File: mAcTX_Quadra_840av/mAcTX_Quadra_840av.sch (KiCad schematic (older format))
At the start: 24 parts, among them J1 ATX-24, J2 39-28-1223, Q1 Q_NPN_BCE

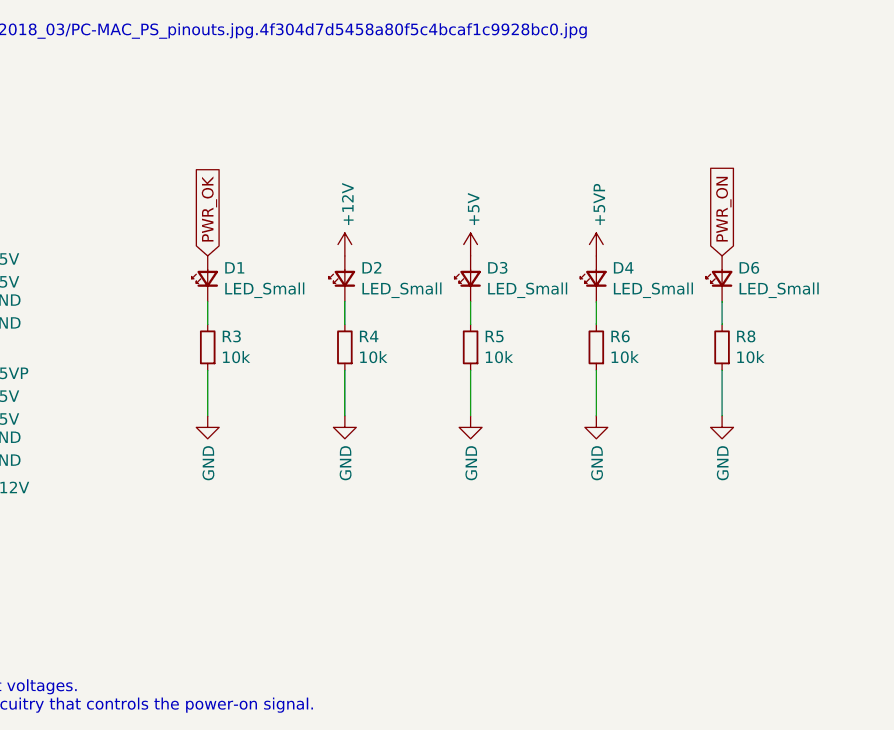
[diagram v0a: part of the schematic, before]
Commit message: Updated schematic to show which parts should not be populated
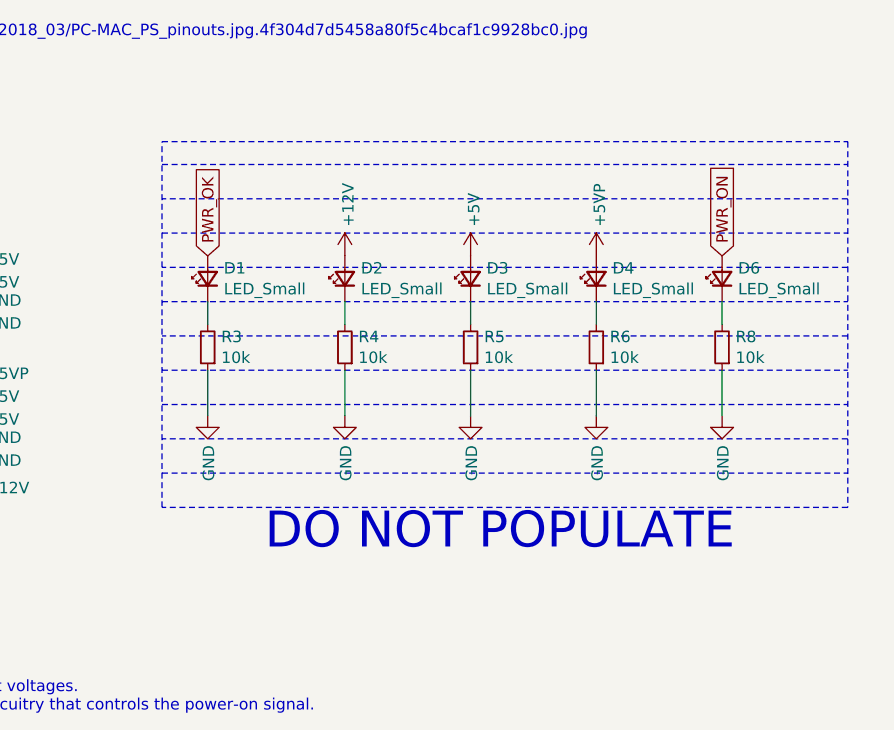
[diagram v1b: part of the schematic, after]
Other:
- note added: "DO NOT POPULATE"
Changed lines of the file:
@@
 	0    1    1    0
 $EndComp
+Wire Notes Line
+	7500 1100 10500 1100
+Wire Notes Line
+	10500 2700 7500 2700
+Wire Notes Line
+	7500 2700 7500 1100
+Wire Notes Line
+	7500 1200 10500 1200
+Wire Notes Line
+	10500 1350 7500 1350
+Wire Notes Line
+	7500 1500 10500 1500
+Wire Notes Line
+	10500 1650 7500 1650
+Wire Notes Line
+	7500 1800 10500 1800
+Wire Notes Line
+	10500 1950 7500 1950
+Wire Notes Line
+	7500 2100 10500 2100
+Wire Notes Line
+	10500 1100 10500 2700
+Wire Notes Line
+	7500 2250 10500 2250
+Wire Notes Line
+	10500 2400 7500 2400
+Wire Notes Line
+	7500 2550 10500 2550
+Text Notes 7950 2900 0    157  ~ 0
+DO NOT POPULATE
 $EndSCHEMATC
